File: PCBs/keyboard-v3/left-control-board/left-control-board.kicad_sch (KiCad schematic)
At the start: 3 parts

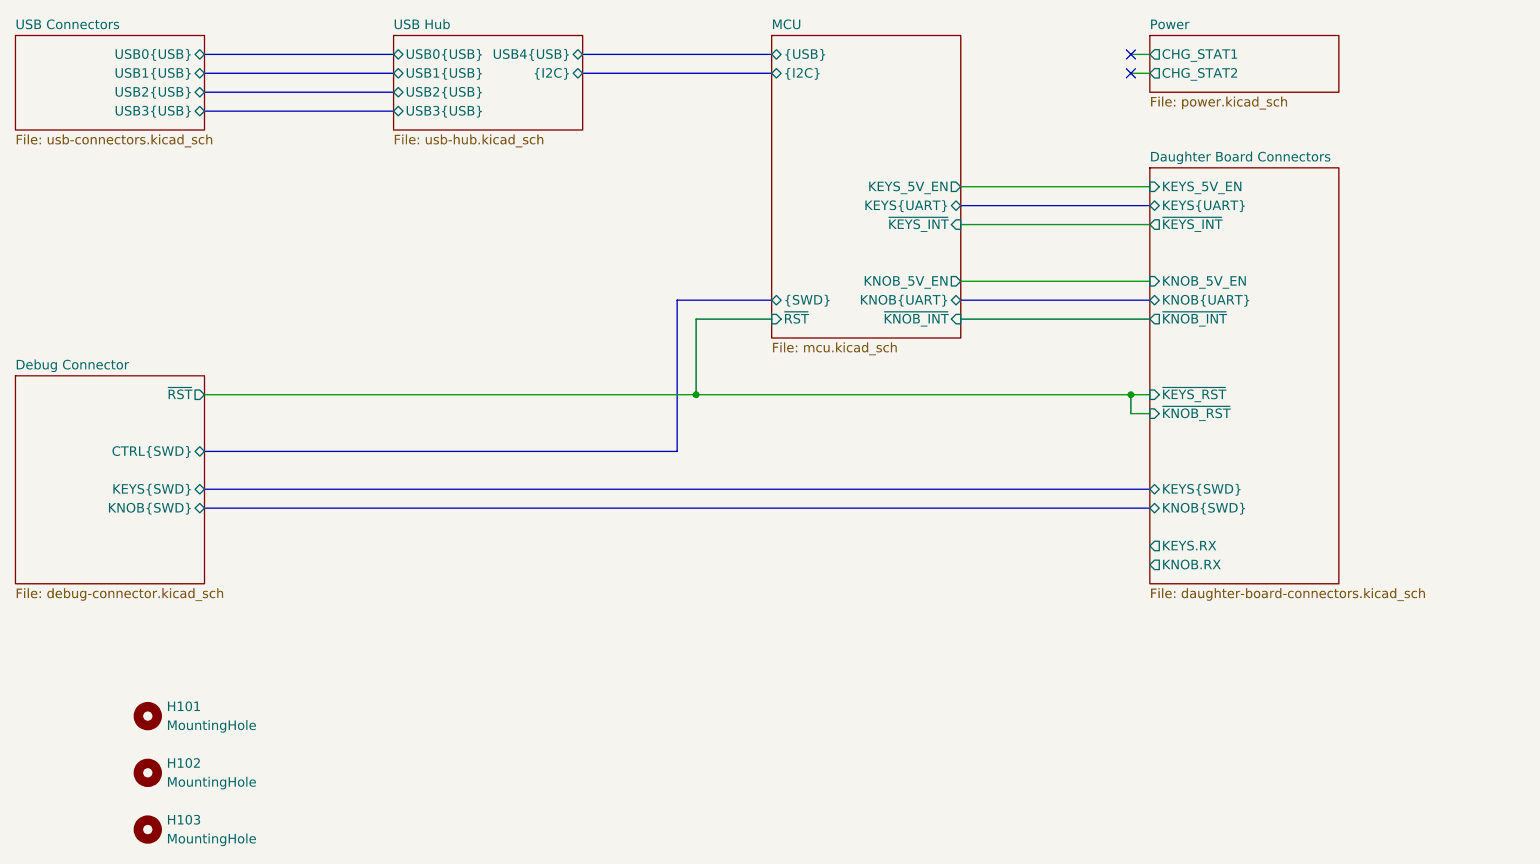
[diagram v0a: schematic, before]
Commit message: Added debug-breakout board, progress on right side schematics & layout
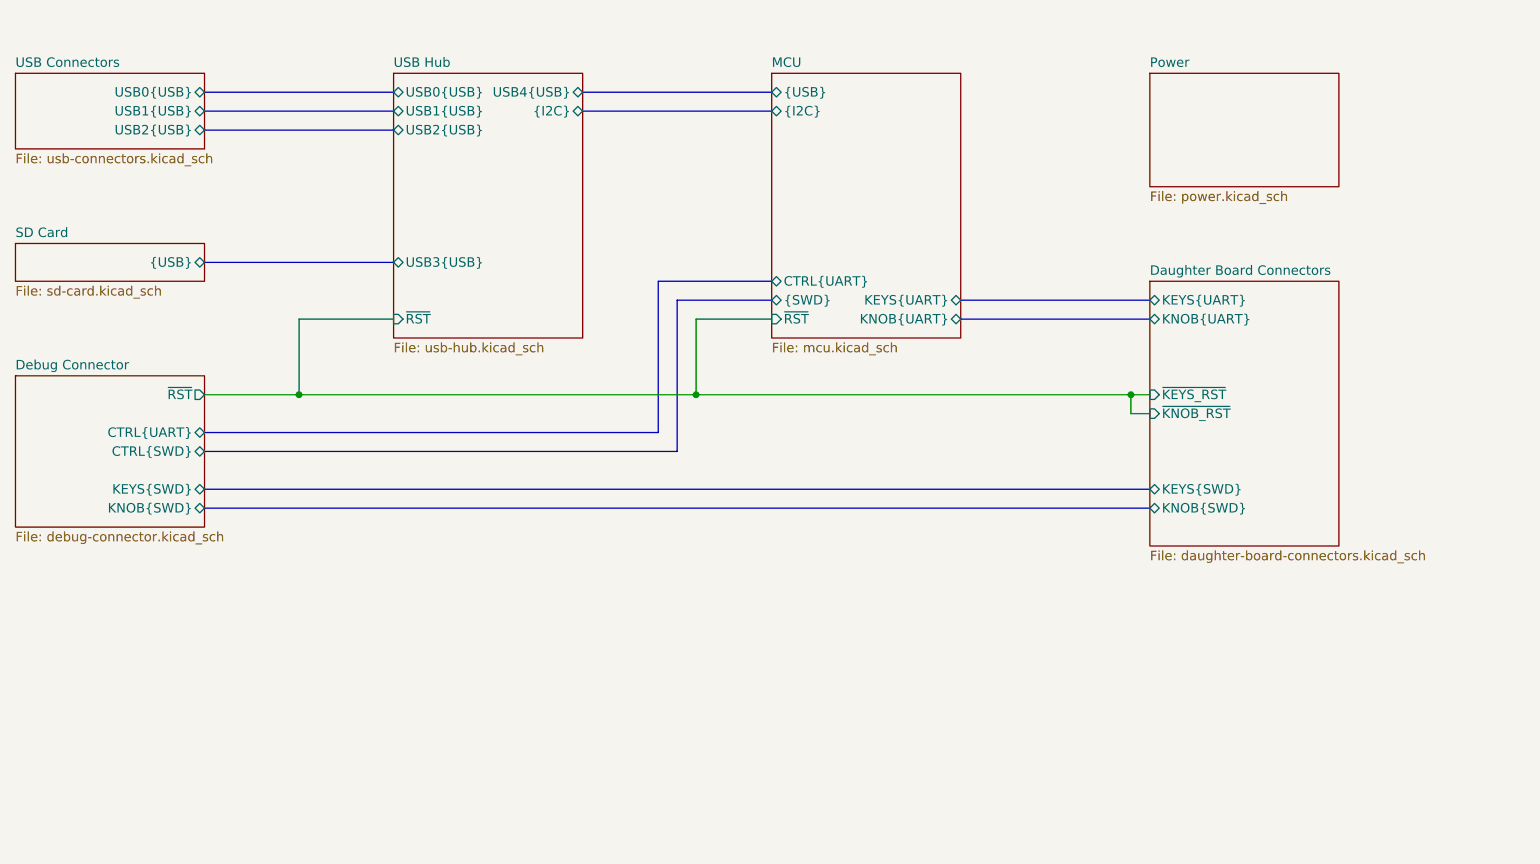
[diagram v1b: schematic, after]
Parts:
- removed H101, H102, H103: MountingHole, MountingHole:MountingHole_2.2mm_M2, symbol Mechanical:MountingHole
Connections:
- no-connect marks 2 -> 0
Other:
- added sheet SD Card (sd-card.kicad_sch)
- sheet Daughter Board Connectors ports: added none; removed KEYS.RX, KEYS_5V_EN, KNOB.RX, KNOB_5V_EN, ~{KEYS_INT}, ~{KNOB_INT}
- sheet Debug Connector ports: added CTRL{UART}; removed none
- sheet MCU ports: added CTRL{UART}; removed KEYS_5V_EN, KNOB_5V_EN, ~{KEYS_INT}, ~{KNOB_INT}
- sheet Power ports: added none; removed CHG_STAT1, CHG_STAT2
- sheet USB Connectors ports: added none; removed USB3{USB}
- sheet USB Hub ports: added ~{RST}; removed none

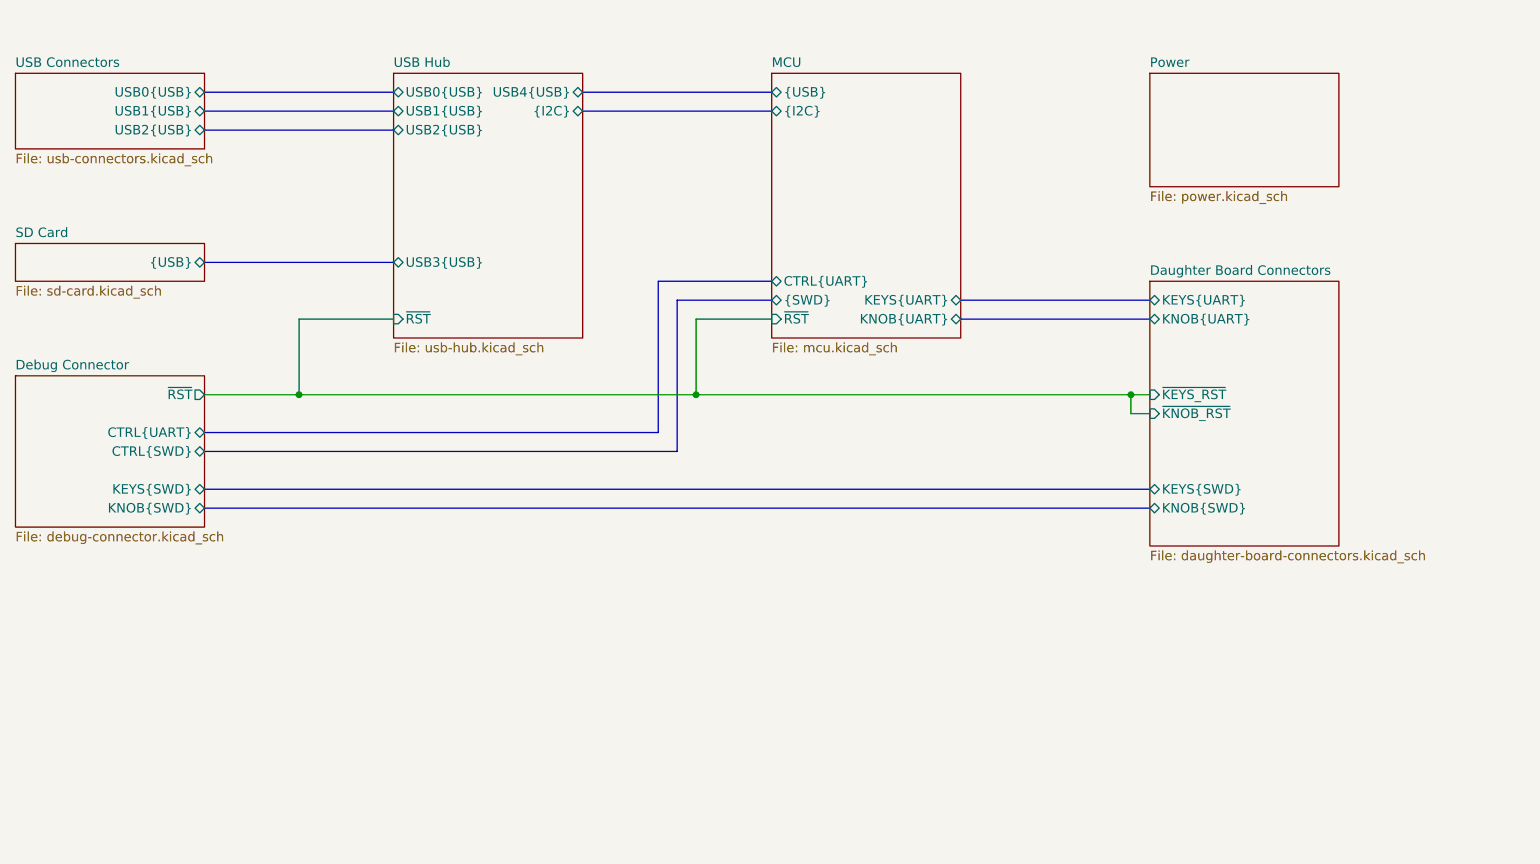
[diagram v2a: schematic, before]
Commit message: Left knob board done
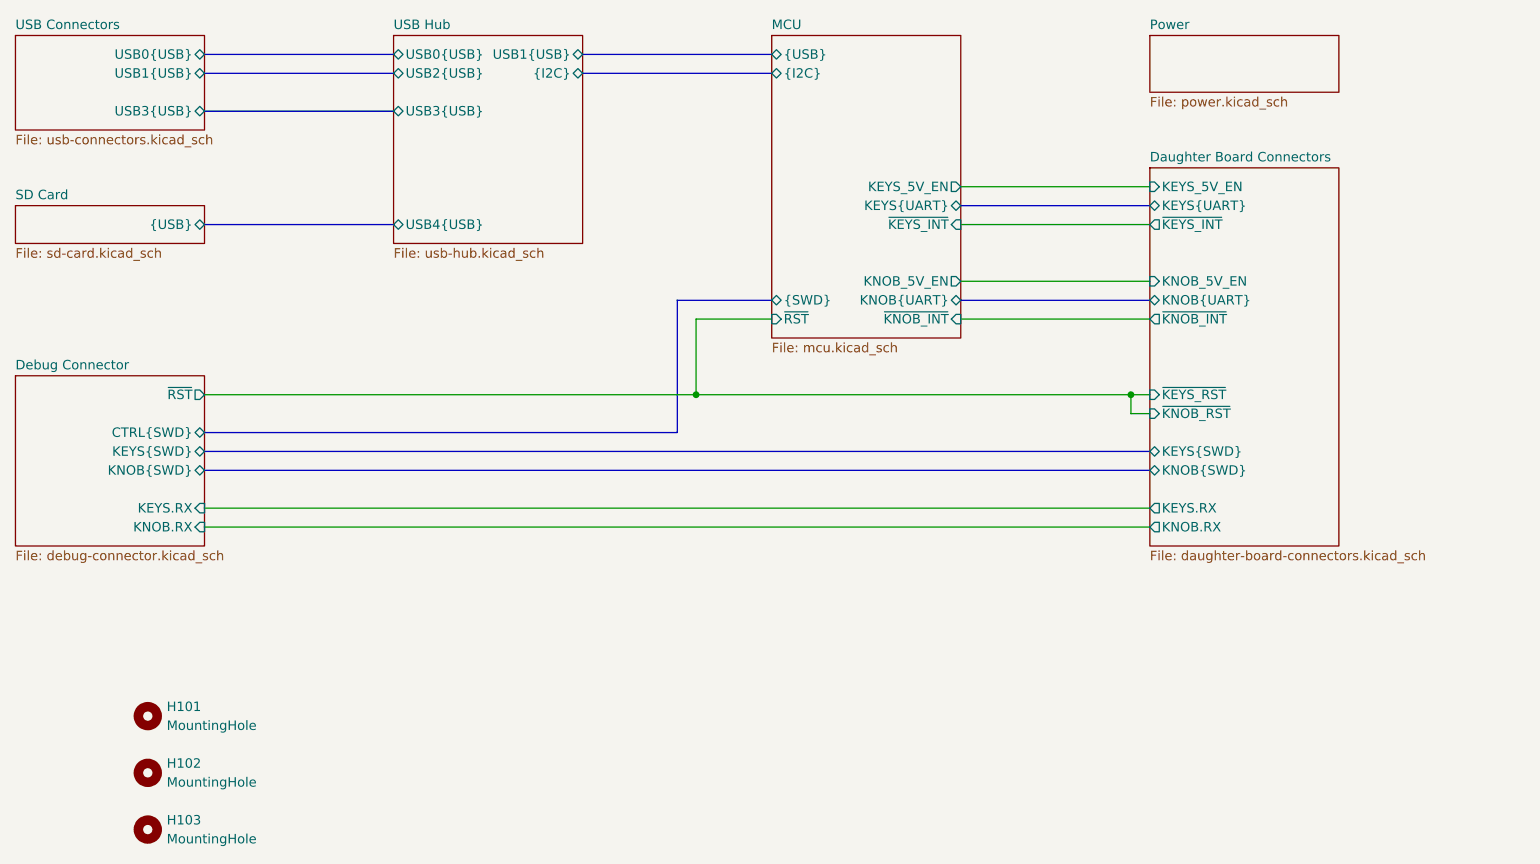
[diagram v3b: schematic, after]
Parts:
- added H101, H102, H103: MountingHole, MountingHole:MountingHole_2.2mm_M2, symbol Mechanical:MountingHole
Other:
- sheet Daughter Board Connectors ports: added KEYS.RX, KEYS_5V_EN, KNOB.RX, KNOB_5V_EN, ~{KEYS_INT}, ~{KNOB_INT}; removed none
- sheet Debug Connector ports: added KEYS.RX, KNOB.RX; removed CTRL{UART}
- sheet MCU ports: added KEYS_5V_EN, KNOB_5V_EN, ~{KEYS_INT}, ~{KNOB_INT}; removed CTRL{UART}
- sheet USB Connectors ports: added USB3{USB}; removed USB2{USB}
- sheet USB Hub ports: added none; removed ~{RST}

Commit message: Keyboard v3 hardware done
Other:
- sheet USB Connectors ports: added USB2{USB}; removed USB1{USB}
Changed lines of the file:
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@@
 	(bus
 		(pts
-			(xy 88.9 63.5) (xy 114.3 63.5)
+			(xy 88.9 66.04) (xy 114.3 66.04)
 		)
 		(stroke
@@
 			)
 		)
-		(pin "USB1{USB}" bidirectional
-			(at 88.9 63.5 0)
+		(pin "USB2{USB}" bidirectional
+			(at 88.9 66.04 0)
 			(effects
 				(font
@@
 		)
 		(pin "USB2{USB}" bidirectional
-			(at 114.3 63.5 180)
-			(effects
-				(font
+			(at 114.3 66.04 180)
+			(effects
+				(font
